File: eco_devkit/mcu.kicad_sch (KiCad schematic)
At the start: 0 parts

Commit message: Update layout
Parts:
- added C1, C2: 15p, Capacitor_SMD:C_0402_1005Metric, symbol Device:C_Small
- added C10, C6, C7, C9: 4.7u, Capacitor_SMD:C_0402_1005Metric, symbol Device:C_Small
- added C11, C12, C13, C14, C15, C16, C17, C18, C19, C20, C4, C8: 100n, Capacitor_SMD:C_0402_1005Metric, symbol Device:C_Small
- added C3, C5: 10u, Capacitor_SMD:C_0402_1005Metric, symbol Device:C_Small
- added D1: SB120, Diode_SMD:D_SOD-123F, symbol Diode:SB120
- added FLASH_MEMORY_8MB1: W25Q80DVSSIG, Package_SON:WSON-8-1EP_6x5mm_P1.27mm_EP3.4x4.3mm, symbol rp2350b-qfn80:Flash_Memory_8MB
- added H1, H2, H3, H4: MountingHole, symbol Mechanical:MountingHole
- added J1: USB_C_Receptacle_USB2.0_16P, lib:UJ20-C-H-G-SMT-1-P16-TR, symbol Connector:USB_C_Receptacle_USB2.0_16P
- added J2: Conn_02x20_Counter_Clockwise, Connector_PinHeader_2.54mm:PinHeader_2x20_P2.54mm_Vertical, symbol Connector_Generic:Conn_02x20_Counter_Clockwise
- added L1: 3.3u, Inductor_SMD:L_0402_1005Metric, symbol Device:L
- added NCP1: NCP1117ST50T3G, lib:NCP1117ST50T3G, symbol rp2350b-qfn80:NCP1117
- added R1, R2: 0, Resistor_SMD:R_0402_1005Metric, symbol Device:R_Small_US
- added R10, R11: 27, Resistor_SMD:R_0402_1005Metric, symbol Device:R_Small_US
- added R3, R4: 5.1k, Resistor_SMD:R_0402_1005Metric, symbol Device:R_Small_US
- added R5: 10k, Resistor_SMD:R_0402_1005Metric, symbol Device:R_Small_US
- added R6, R7, R9: 1k, Resistor_SMD:R_0402_1005Metric, symbol Device:R_Small_US
- added R8: 33, Resistor_SMD:R_0402_1005Metric, symbol Device:R_Small_US
- added RP2350B1: RP2350B1, lib:RP2350B_QFN-80_EP_10.573x10.573_Pitch0.4mm, symbol rp2350b-qfn80:RP2350B-QFN80
- added SW1: BOOT, Button_Switch_SMD:SW_Tactile_SPST_NO_Straight_CK_PTS636Sx25SMTRLFS, symbol Switch:SW_Push
- added SW2: RESET, Button_Switch_SMD:SW_Tactile_SPST_NO_Straight_CK_PTS636Sx25SMTRLFS, symbol Switch:SW_Push
- added Y1: Crystal_GND24, lib:ABM8-272-T3, symbol Device:Crystal_GND24
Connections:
- new net: R10.1, RP2350B1.67 (USB_DP)
- new net: C10.1, R8.2, RP2350B1.61 (VREG_AVDD)
- new net: L1.2, RP2350B1.63 (VREG_LX)
- new net: R11.1, RP2350B1.66 (USB_DM)
- new net: R9.1, SW1.2
- new net: FLASH_MEMORY_8MB1.1 (/CS), R1.2, R2.2, R5.2
- new net: C2.2, R6.1, Y1.3
- new net: R7.2, SW2.1
- new net: D1.2 (A), J1.A4 (VBUS), J1.A9 (VBUS), J1.B4 (VBUS), J1.B9 (VBUS)
- new net: J1.A5 (CC1), R3.1
- new net: J1.B5 (CC2), R4.1
- new net +1V1: C11.1, C7.1, C8.1, C9.1, J2.2 (Pin_2), L1.1, RP2350B1.10 (DVDD), RP2350B1.32 (DVDD), RP2350B1.51 (DVDD), RP2350B1.65 (VREG_FB)
- new net +3V3: C12.1, C13.1, C14.1, C15.1, C16.1, C17.1, C18.1, C19.1, C20.1, C4.1, C5.1, C6.1, FLASH_MEMORY_8MB1.8 (VCC), J2.1 (Pin_1), NCP1.2 (VO), R5.1, R8.1, RP2350B1.15 (IOVDD), RP2350B1.24 (IOVDD), RP2350B1.29 (IOVDD), RP2350B1.41 (IOVDD), RP2350B1.5 (IOVDD), RP2350B1.50 (IOVDD), RP2350B1.59 (ADC_AVDD), RP2350B1.60 (IOVDD), RP2350B1.64 (VREG_VIN), RP2350B1.68 (USB_OTP_VDD), RP2350B1.69 (QSPI_IOVDD), RP2350B1.76 (IOVDD)
- new net +VBUS: C3.1, D1.1 (K), J2.3 (Pin_3), NCP1.3 (VI)
- new net ACCEL_CS: RP2350B1.28 (GPIO27)
- new net ACCEL_INT1: RP2350B1.36 (GPIO28)
- new net ACCEL_INT2: RP2350B1.37 (GPIO29)
- new net ACCEL_MISO: J2.37 (Pin_37), RP2350B1.20 (GPIO20)
- new net ACCEL_MOSI: J2.38 (Pin_38), RP2350B1.19 (GPIO19)
- new net ACCEL_SCK: J2.39 (Pin_39), RP2350B1.18 (GPIO18)
- new net DISPLAY_EN: J2.17 (Pin_17), RP2350B1.12 (GPIO13)
- new net DISPLAY_MOSI: J2.15 (Pin_15), RP2350B1.9 (GPIO11)
- new net DISPLAY_RST: J2.16 (Pin_16), RP2350B1.11 (GPIO12)
- new net DISPLAY_SCK: J2.14 (Pin_14), RP2350B1.8 (GPIO10)
- new net GND: C1.1, C10.2, C11.2, C12.2, C13.2, C14.2, C15.2, C16.2, C17.2, C18.2, C19.2, C2.1, C20.2, C3.2, C4.2, C5.2, C6.2, C7.2, C8.2, C9.2, FLASH_MEMORY_8MB1.4 (GND), J1.A1 (GND), J1.A12 (GND), J1.B1 (GND), J1.B12 (GND), J2.4 (Pin_4), NCP1.1 (GND), R3.2, R4.2, R7.1, RP2350B1.62 (VREG_PGND), RP2350B1.81 (GND), SW1.1, Y1.2, Y1.4
- new net GPIO14: J2.18 (Pin_18), RP2350B1.13 (GPIO14)
- new net GPIO15: J2.19 (Pin_19), RP2350B1.14 (GPIO15)
- new net GPIO16: J2.20 (Pin_20), RP2350B1.16 (GPIO16)
- new net GPIO17: J2.40 (Pin_40), RP2350B1.17 (GPIO17)
- new net GPIO2: J2.6 (Pin_6), RP2350B1.79 (GPIO2)
- new net GPIO21: J2.36 (Pin_36), RP2350B1.21 (GPIO21)
- new net GPIO22: RP2350B1.22 (GPIO22)
- new net GPIO23: J2.35 (Pin_35), RP2350B1.23 (GPIO23)
- new net GPIO24: J2.34 (Pin_34), RP2350B1.25 (GPIO24)
- new net GPIO25: J2.33 (Pin_33), RP2350B1.26 (GPIO25)
- new net GPIO3: J2.7 (Pin_7), RP2350B1.80 (GPIO3)
- new net GPIO40_ADC0: J2.31 (Pin_31), RP2350B1.49 (GPIO40_ADC0)
- new net GPIO41_ADC1: J2.30 (Pin_30), RP2350B1.52 (GPIO41_ADC1)
- new net GPIO42_ADC2: J2.29 (Pin_29), RP2350B1.53 (GPIO42_ADC2)
- new net GPIO43_ADC3: J2.24 (Pin_24), J2.28 (Pin_28), RP2350B1.54 (GPIO43_ADC3), RP2350B1.58 (GPIO47_ADC7)
- new net GPIO44_ADC4: J2.27 (Pin_27), RP2350B1.55 (GPIO44_ADC4)
- new net GPIO45_ADC5: J2.26 (Pin_26), RP2350B1.56 (GPIO45_ADC5)
- new net GPIO46_ADC6: J2.25 (Pin_25), RP2350B1.57 (GPIO46_ADC6)
- new net GPIO6: J2.10 (Pin_10), RP2350B1.3 (GPIO6)
- new net GPIO_MOSFET_GATE_IN: RP2350B1.38 (GPIO30)
- new net PIN_ADDRESSABE: RP2350B1.44 (GPIO35)
- new net PIN_BTN1: RP2350B1.45 (GPIO36)
- new net PIN_BTN2: RP2350B1.46 (GPIO37)
- new net PIN_BTN3: RP2350B1.47 (GPIO38)
- new net PIN_BTN4: RP2350B1.48 (GPIO39)
- new net PIN_BUZZER: J2.32 (Pin_32), RP2350B1.27 (GPIO26)
- new net PIN_LED_BLUE: RP2350B1.42 (GPIO33)
- new net PIN_LED_GREEN: RP2350B1.40 (GPIO32)
- new net PIN_LED_RED: RP2350B1.39 (GPIO31)
- new net PIN_LED_YELLOW: RP2350B1.43 (GPIO34)
- new net PIN_LIGHT_SENS_SCL: J2.9 (Pin_9), RP2350B1.2 (GPIO5)
- new net PIN_LIGHT_SENS_SDA: J2.8 (Pin_8), RP2350B1.1 (GPIO4)
- new net PIN_WIFI_RESET_BL: J2.11 (Pin_11), RP2350B1.4 (GPIO7)
- new net PIN_WIFI_RX: J2.12 (Pin_12), RP2350B1.6 (GPIO8)
- new net PIN_WIFI_TX: J2.13 (Pin_13), RP2350B1.7 (GPIO9)
- new net POBRE_GPIO3/SWDIO: RP2350B1.34 (SWDIO)
- new net POBRE_GPIO5/UART_RX: J2.5 (Pin_5), RP2350B1.78 (GPIO1)
- new net PROBE_GPIO2/SWCLK: J2.21 (Pin_21), RP2350B1.33 (SWCLK)
- new net PROBE_GPIO4/UART_TX: R1.1, RP2350B1.77 (GPIO0)
- new net QSPI_SCLK: FLASH_MEMORY_8MB1.6 (CLK), RP2350B1.71 (QSPI_SCLK)
- new net QSPI_SD0: FLASH_MEMORY_8MB1.5 (DI_(IO0)), RP2350B1.72 (QSPI_SD0)
- new net QSPI_SD1: FLASH_MEMORY_8MB1.2 (DO_(IO1)), RP2350B1.74 (QSPI_SD1)
- new net QSPI_SD2: FLASH_MEMORY_8MB1.3 (/WP_(IO2)), RP2350B1.73 (QSPI_SD2)
- new net QSPI_SD3: FLASH_MEMORY_8MB1.7 (/HOLD_(IO3)), RP2350B1.70 (QSPI_SD3)
- new net QSPI_SS: R2.1, R9.2, RP2350B1.75 (QSPI_SS)
- new net RUN: J2.23 (Pin_23), RP2350B1.35 (RUN), SW2.2
- new net SWD: J2.22 (Pin_22)
- new net USB_D+: J1.A6 (D+), J1.B6 (D+), R10.2
- new net USB_D-: J1.A7 (D-), J1.B7 (D-), R11.2
- new net XIN: C1.2, Y1.1
- new net XOUT: R6.2, RP2350B1.30 (XIN), RP2350B1.31 (XOUT)
- no-connect marks 0 -> 4
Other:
- note added: "12MHz Crystal"
- note added: "ACCEL SPI"
- note added: "DISPLAY SPI"
- note added: "FLASH MEMORY 8MB"
- note added: "GPIO PINHEADER"
- note added: "MCU"
- note added: "MCU RP2350"
- note added: "POWER USB-C"
- note added: "RP2350B"
- note added: "SDCARD SPI"

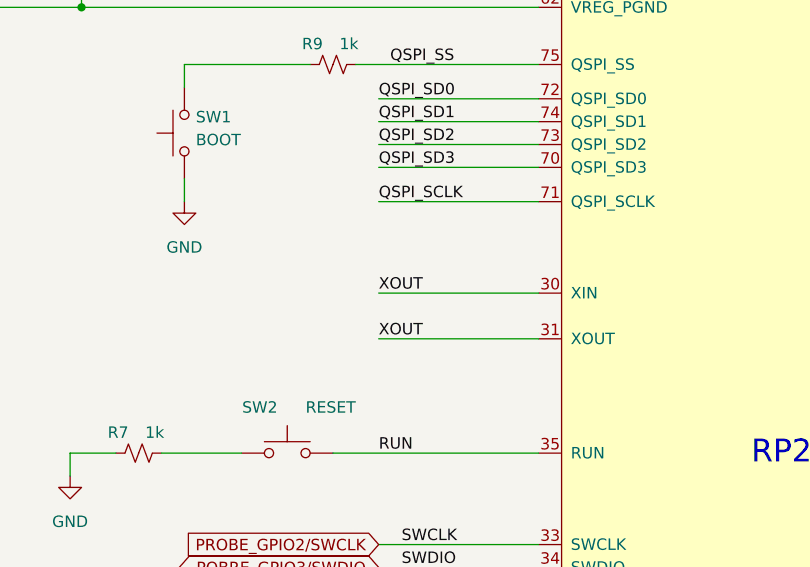
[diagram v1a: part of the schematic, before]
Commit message: feat: placement of MCU passive components and crystal
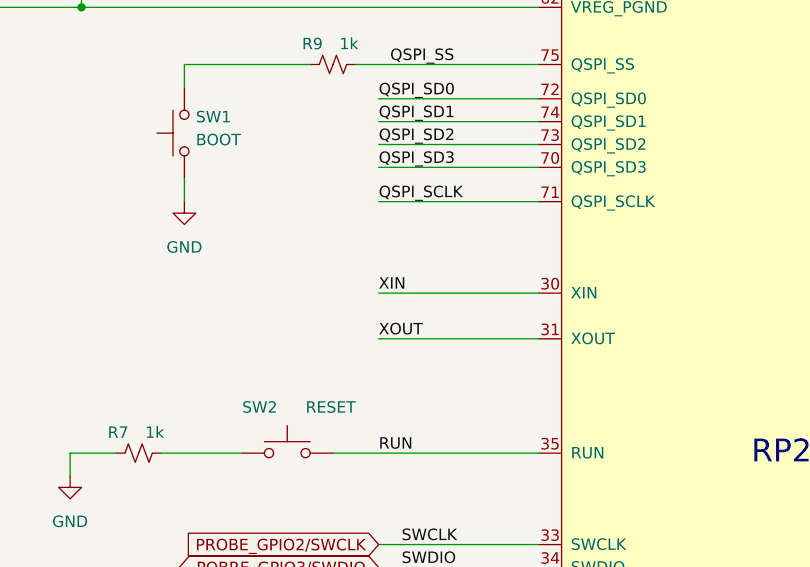
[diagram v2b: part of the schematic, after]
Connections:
- net XIN: now also RP2350B1.30 (XIN)
- net XOUT: no longer RP2350B1.30 (XIN)
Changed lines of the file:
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@@
 		)
 	)
-	(label "XOUT"
+	(label "XIN"
 		(at 303.53 214.63 0)
 		(effects

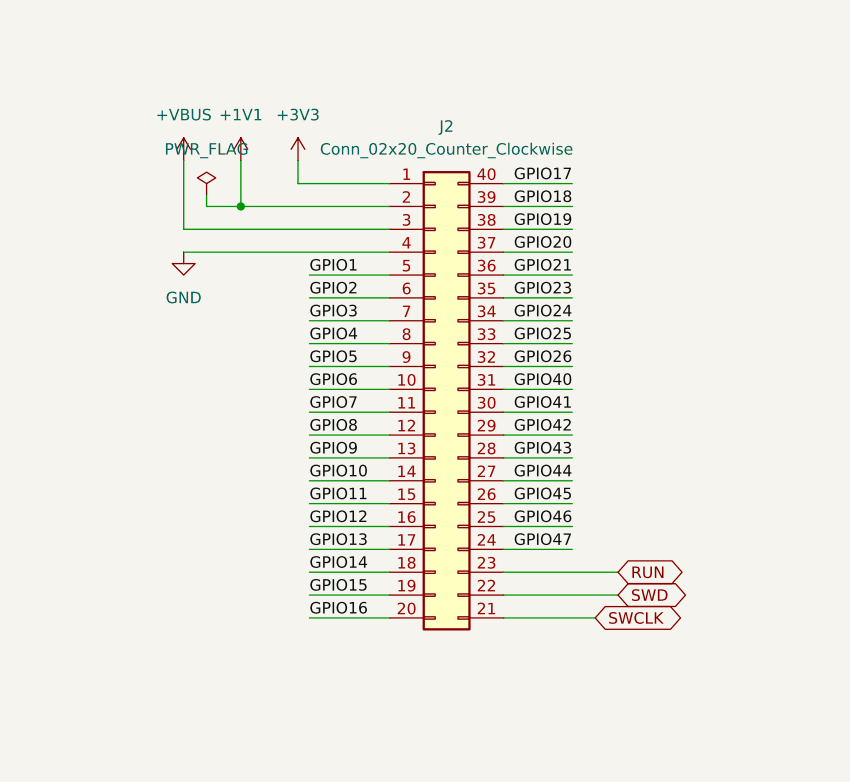
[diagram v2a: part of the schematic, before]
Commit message: feat: MCU placement and routing of power and signal connections
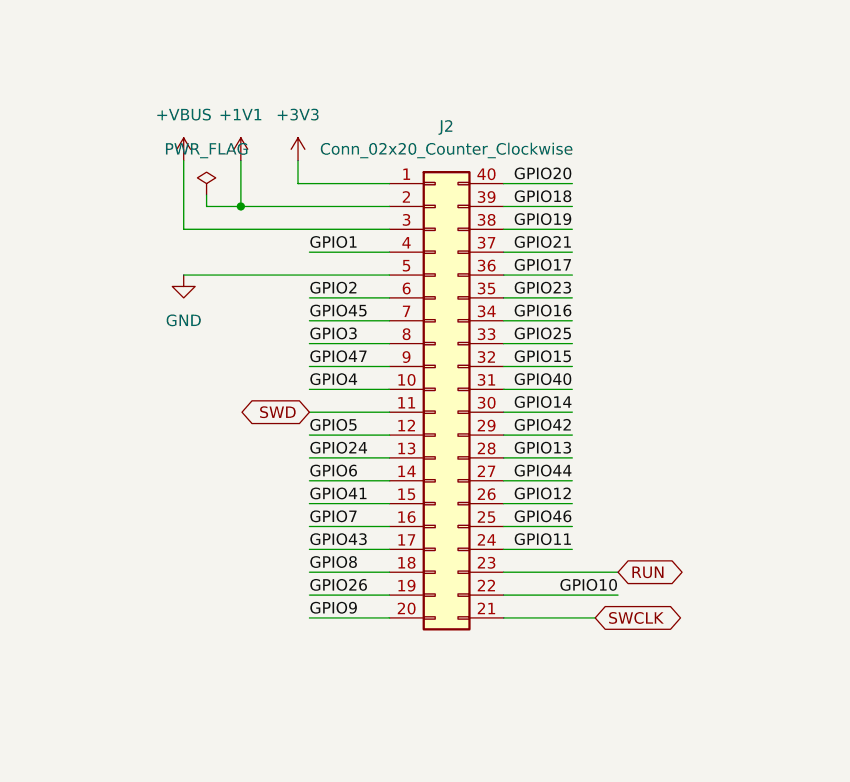
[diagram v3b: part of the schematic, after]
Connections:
- net ACCEL_MISO: now also J2.40 (Pin_40); no longer J2.37 (Pin_37)
- net DISPLAY_EN: now also J2.28 (Pin_28); no longer J2.17 (Pin_17)
- net DISPLAY_MOSI: now also J2.24 (Pin_24); no longer J2.15 (Pin_15)
- net DISPLAY_RST: now also J2.26 (Pin_26); no longer J2.16 (Pin_16)
- net DISPLAY_SCK: now also J2.22 (Pin_22); no longer J2.14 (Pin_14)
- net GND: now also J2.5 (Pin_5); no longer J2.4 (Pin_4)
- net GPIO14: now also J2.30 (Pin_30); no longer J2.18 (Pin_18)
- net GPIO15: now also J2.32 (Pin_32); no longer J2.19 (Pin_19)
- net GPIO16: now also J2.34 (Pin_34); no longer J2.20 (Pin_20)
- net GPIO17: now also J2.36 (Pin_36); no longer J2.40 (Pin_40)
- net GPIO21: now also J2.37 (Pin_37); no longer J2.36 (Pin_36)
- net GPIO24: now also J2.13 (Pin_13); no longer J2.34 (Pin_34)
- net GPIO3: now also J2.8 (Pin_8); no longer J2.7 (Pin_7)
- net GPIO41_ADC1: now also J2.15 (Pin_15); no longer J2.30 (Pin_30)
- net GPIO43_ADC3: now also J2.17 (Pin_17), J2.9 (Pin_9); no longer J2.24 (Pin_24), J2.28 (Pin_28)
- net GPIO45_ADC5: now also J2.7 (Pin_7); no longer J2.26 (Pin_26)
- net GPIO6: now also J2.14 (Pin_14); no longer J2.10 (Pin_10)
- net PIN_BUZZER: now also J2.19 (Pin_19); no longer J2.32 (Pin_32)
- net PIN_LIGHT_SENS_SCL: now also J2.12 (Pin_12); no longer J2.9 (Pin_9)
- net PIN_LIGHT_SENS_SDA: now also J2.10 (Pin_10); no longer J2.8 (Pin_8)
- net PIN_WIFI_RESET_BL: now also J2.16 (Pin_16); no longer J2.11 (Pin_11)
- net PIN_WIFI_RX: now also J2.18 (Pin_18); no longer J2.12 (Pin_12)
- net PIN_WIFI_TX: now also J2.20 (Pin_20); no longer J2.13 (Pin_13)
- net POBRE_GPIO5/UART_RX: now also J2.4 (Pin_4); no longer J2.5 (Pin_5)
- net SWD: now also J2.11 (Pin_11); no longer J2.22 (Pin_22)
